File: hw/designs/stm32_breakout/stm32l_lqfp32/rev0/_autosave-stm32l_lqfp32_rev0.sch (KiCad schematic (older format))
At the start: 18 parts, among them J1 USB_B_Micro, U1 LM3670MF, U3 KC2016Z

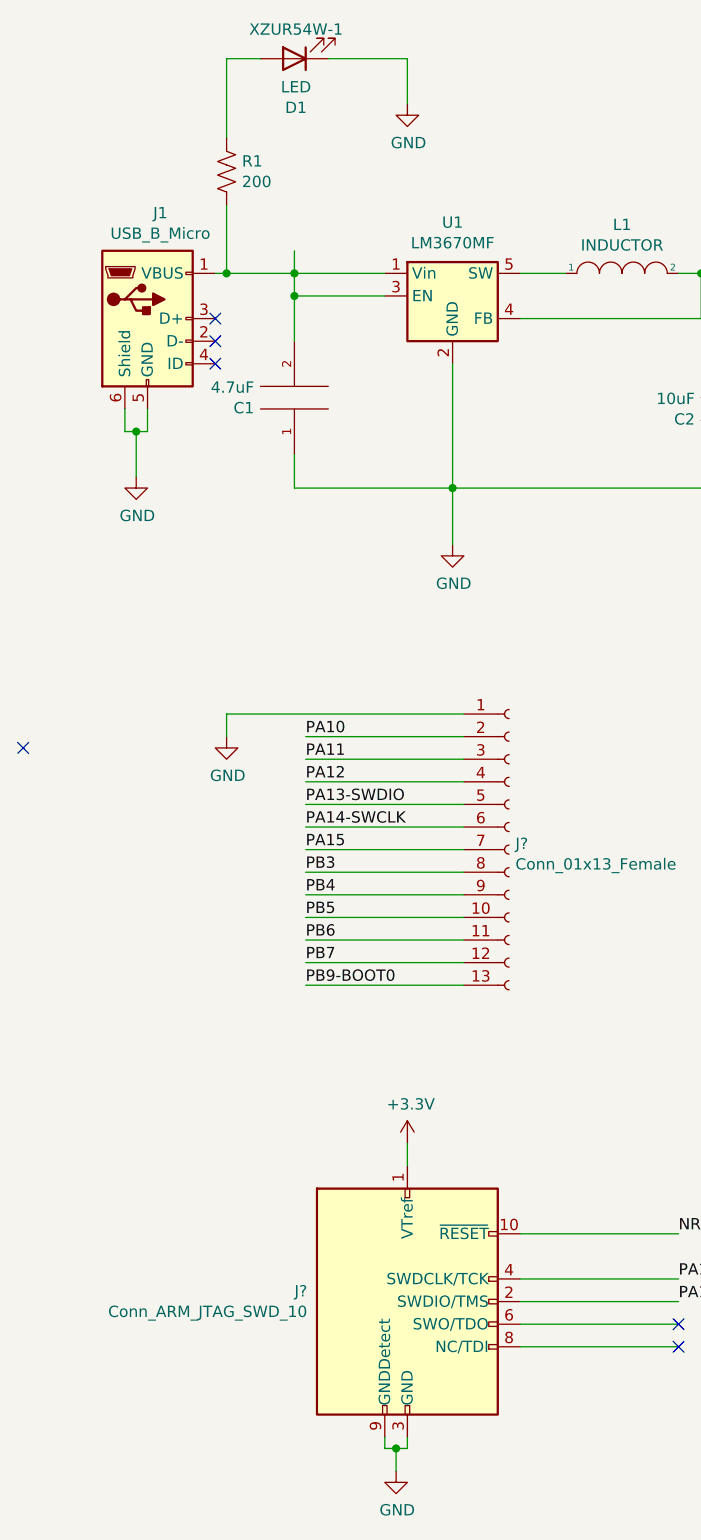
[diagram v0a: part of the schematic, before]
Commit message: Updated some part numbers
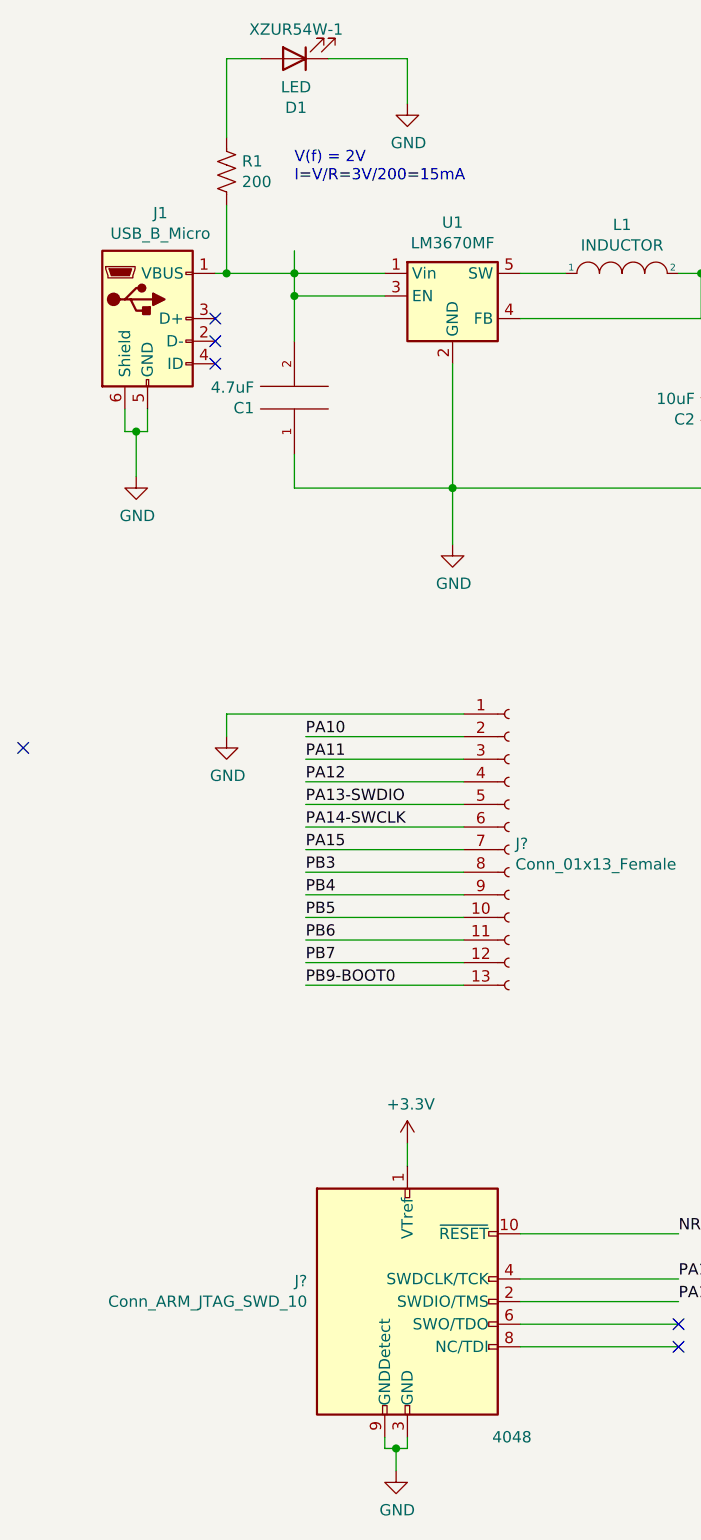
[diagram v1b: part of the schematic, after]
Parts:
- J?: Part_Number (none) -> 4048
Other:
- note added: "V(f) = 2V\nI=V/R=3V/200=15mA"
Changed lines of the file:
@@
 U 1 1 61724BF9
 P 2600 6400
-F 0 "J?" H 2157 6446 50  0000 R CNN
-F 1 "Conn_ARM_JTAG_SWD_10" H 2157 6355 50  0000 R CNN
+F 0 "J?" H 2157 6491 50  0000 R CNN
+F 1 "Conn_ARM_JTAG_SWD_10" H 2157 6400 50  0000 R CNN
 F 2 "" H 2600 6400 50  0001 C CNN
-F 3 "http://infocenter.arm.com/help/topic/com.arm.doc.ddi0314h/DDI0314H_coresight_components_trm.pdf" V 2250 5150 50  0001 C CNN
+F 3 "https://www.adafruit.com/product/4048#description" V 2250 5150 50  0001 C CNN
+F 4 "4048" H 3150 5800 50  0000 R CNN "Part_Number"
 	1    2600 6400
 	1    0    0    -1
@@
 Wire Wire Line
 	2600 900  2600 1100
+Text Notes 2100 1450 0    50   ~ 0
+V(f) = 2V\nI=V/R=3V/200=15mA
 $EndSCHEMATC
